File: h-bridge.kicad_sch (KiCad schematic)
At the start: 20 parts, among them J4 Conn_02x06_Counter_Clockwise, M3 DC, Q10 Q_NMOS, Q7 Q_NMOS, Q8 Q_NMOS, Q9 Q_NMOS, U11 DRV8701

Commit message: schem: add ordering info to BOM
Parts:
- C38, C39, C41: Basic (none) -> Y; JLCPCB Part # (none) -> C52923; Manufacturer (none) -> Samsung Electro-Mechanics; Manufacturer Part Number (none) -> CL05A105KA5NQNC
- C40: Basic (none) -> Y; JLCPCB Part # (none) -> C307331; Manufacturer (none) -> Samsung Electro-Mechanics; Manufacturer Part Number (none) -> CL05B104KB54PNC
- J4, M3: now left out of the parts list
- Q10, Q7, Q8, Q9: Basic (none) -> X; JLCPCB Part # (none) -> C111309; Manufacturer (none) -> Vishay Intertech; Manufacturer Part Number (none) -> SIS412DN-T1-GE3
- R41, R44, R47: Basic (none) -> Y; JLCPCB Part # (none) -> C25744; Manufacturer (none) -> Uniroyal Elec; Manufacturer Part Number (none) -> 0402WGF1002TCE
- R42: Basic (none) -> Y; JLCPCB Part # (none) -> C25779; Manufacturer (none) -> Uniroyal Elec; Manufacturer Part Number (none) -> 0402WGF3302TCE
- R43: Basic (none) -> Y; JLCPCB Part # (none) -> C25764; Manufacturer (none) -> Uniroyal Elec; Manufacturer Part Number (none) -> 0402WGF2003TCE
- R45: Basic (none) -> Y; JLCPCB Part # (none) -> C36871; Manufacturer (none) -> Uniroyal Elec; Manufacturer Part Number (none) -> 0402WGF6802TCE
- R46: footprint Resistor_SMD:R_0402_1005Metric -> Resistor_SMD:R_0603_1608Metric; Basic (none) -> Y; JLCPCB Part # (none) -> C23234; Manufacturer (none) -> Uniroyal Elec; Manufacturer Part Number (none) -> 0603WAF7501T5E
- R48: Basic (none) -> X; JLCPCB Part # (none) -> C5375467; Manufacturer (none) -> Milliohm; Manufacturer Part Number (none) -> HoYLR2512-3W-20mR-1%
- U11: Basic (none) -> X; JLCPCB Part # (none) -> C90964; Manufacturer (none) -> Texas Instruments; Manufacturer Part Number (none) -> DRV8701ERGER

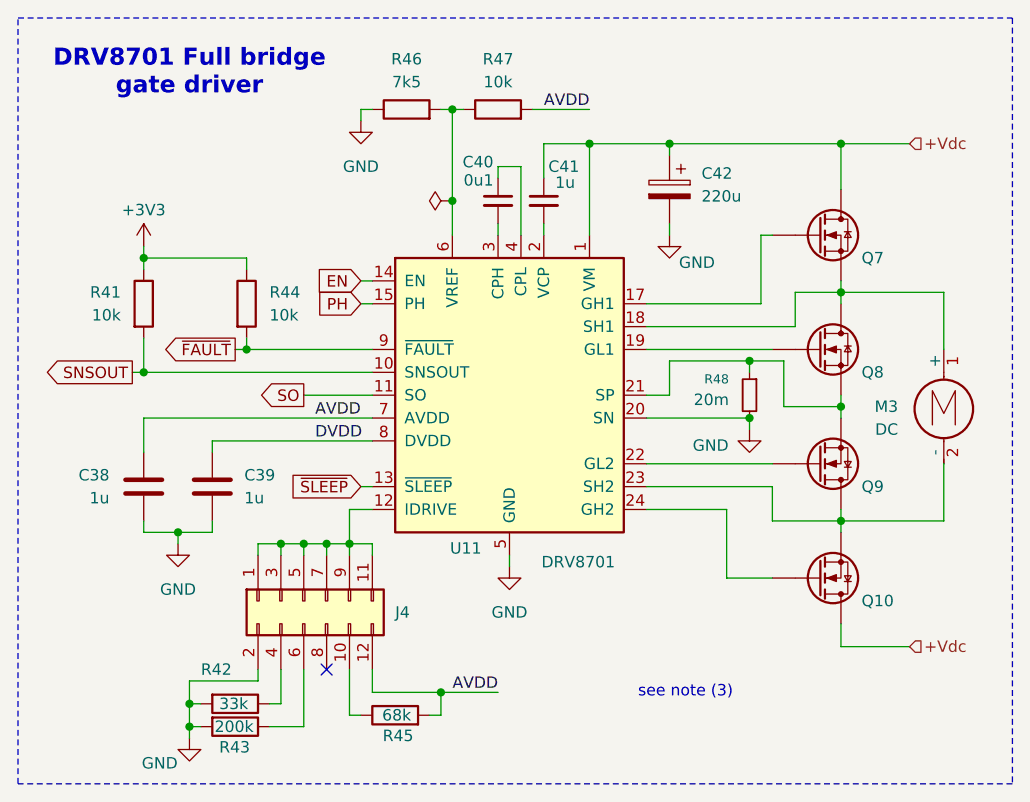
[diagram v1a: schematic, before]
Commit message: schem: renumber
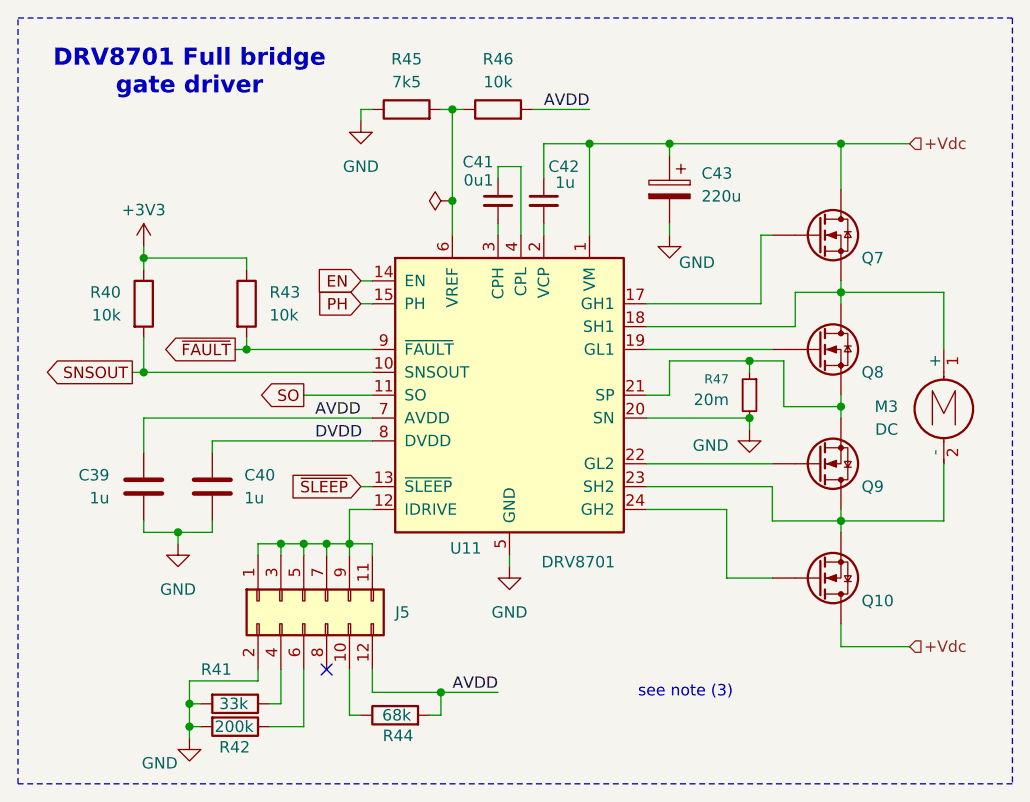
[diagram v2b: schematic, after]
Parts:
- renumbered C38 to C39, C39 to C40, C40 to C41, C41 to C42, C42 to C43, J4 to J5, R41 to R40, R42 to R41, R43 to R42, R44 to R43, R45 to R44, R46 to R45, R47 to R46, R48 to R47
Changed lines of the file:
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@@
 		(dnp no)
 		(fields_autoplaced yes)
-		(property "Reference" "#PWR082"
+		(property "Reference" "#PWR085"
 			(at 130.81 62.23 0)
 			(effects
@@
 			(project ""
 				(path "/a1dc4c9e-7b20-4b66-a693-9133bc644c6b/234f18ec-899d-4a38-bb51-5ceaab0ae171"
-					(reference "#PWR082")
+					(reference "#PWR085")
 					(unit 1)
 				)
@@
 		(on_board yes)
 		(dnp no)
-		(property "Reference" "R47"
+		(property "Reference" "R46"
 			(at 146.05 49.022 90)
 			(effects
@@
 			(project ""
 				(path "/a1dc4c9e-7b20-4b66-a693-9133bc644c6b/234f18ec-899d-4a38-bb51-5ceaab0ae171"
-					(reference "R47")
+					(reference "R46")
 					(unit 1)
 				)
@@
 		(on_board yes)
 		(dnp no)
-		(property "Reference" "C38"
+		(property "Reference" "C39"
 			(at 102.87 95.2499 0)
 			(effects
@@
 			(project ""
 				(path "/a1dc4c9e-7b20-4b66-a693-9133bc644c6b/234f18ec-899d-4a38-bb51-5ceaab0ae171"
-					(reference "C38")
+					(reference "C39")
 					(unit 1)
 				)
@@
 		(on_board yes)
 		(dnp no)
-		(property "Reference" "R43"
+		(property "Reference" "R42"
 			(at 115.062 125.476 90)
 			(effects
@@
 			(project "motor-power-poc"
 				(path "/a1dc4c9e-7b20-4b66-a693-9133bc644c6b/234f18ec-899d-4a38-bb51-5ceaab0ae171"
-					(reference "R43")
+					(reference "R42")
 					(unit 1)
 				)
@@
 		(on_board yes)
 		(dnp no)
-		(property "Reference" "C39"
+		(property "Reference" "C40"
 			(at 117.856 95.25 0)
 			(effects
@@
 			(project "motor-power-poc"
 				(path "/a1dc4c9e-7b20-4b66-a693-9133bc644c6b/234f18ec-899d-4a38-bb51-5ceaab0ae171"
-					(reference "C39")
+					(reference "C40")
 					(unit 1)
 				)
@@
 		(on_board yes)
 		(dnp no)
-		(property "Reference" "C41"
+		(property "Reference" "C42"
 			(at 151.638 60.96 0)
 			(effects
@@
 			(project "motor-power-poc"
 				(path "/a1dc4c9e-7b20-4b66-a693-9133bc644c6b/234f18ec-899d-4a38-bb51-5ceaab0ae171"
-					(reference "C41")
+					(reference "C42")
 					(unit 1)
 				)
@@
 		(on_board yes)
 		(dnp no)
-		(property "Reference" "R46"
+		(property "Reference" "R45"
 			(at 135.89 49.022 90)
 			(effects
@@
 			(project "motor-power-poc"
 				(path "/a1dc4c9e-7b20-4b66-a693-9133bc644c6b/234f18ec-899d-4a38-bb51-5ceaab0ae171"
-					(reference "R46")
+					(reference "R45")
 					(unit 1)
 				)
@@
 		(on_board yes)
 		(dnp no)
-		(property "Reference" "C42"
+		(property "Reference" "C43"
 			(at 168.656 61.722 0)
 			(effects
@@
 			(project "motor-power-poc"
 				(path "/a1dc4c9e-7b20-4b66-a693-9133bc644c6b/234f18ec-899d-4a38-bb51-5ceaab0ae171"
-					(reference "C42")
+					(reference "C43")
 					(unit 1)
 				)
@@
 		(dnp no)
 		(fields_autoplaced yes)
-		(property "Reference" "#PWR080"
+		(property "Reference" "#PWR083"
 			(at 110.49 109.22 0)
 			(effects
@@
 			(project "motor-power-poc"
 				(path "/a1dc4c9e-7b20-4b66-a693-9133bc644c6b/234f18ec-899d-4a38-bb51-5ceaab0ae171"
-					(reference "#PWR080")
+					(reference "#PWR083")
 					(unit 1)
 				)
@@
 		(on_board yes)
 		(dnp no)
-		(property "Reference" "R48"
+		(property "Reference" "R47"
 			(at 171.704 84.582 0)
 			(effects
@@
 			(project ""
 				(path "/a1dc4c9e-7b20-4b66-a693-9133bc644c6b/234f18ec-899d-4a38-bb51-5ceaab0ae171"
-					(reference "R48")
+					(reference "R47")
 					(unit 1)
 				)
@@
 		(on_board yes)
 		(dnp no)
-		(property "Reference" "R45"
+		(property "Reference" "R44"
 			(at 136.652 124.206 90)
 			(effects
@@
 			(project "motor-power-poc"
 				(path "/a1dc4c9e-7b20-4b66-a693-9133bc644c6b/234f18ec-899d-4a38-bb51-5ceaab0ae171"
-					(reference "R45")
+					(reference "R44")
 					(unit 1)
 				)
@@
 		(dnp no)
 		(fields_autoplaced yes)
-		(property "Reference" "J4"
+		(property "Reference" "J5"
 			(at 134.62 110.4899 90)
 			(effects
@@
 			(project ""
 				(path "/a1dc4c9e-7b20-4b66-a693-9133bc644c6b/234f18ec-899d-4a38-bb51-5ceaab0ae171"
-					(reference "J4")
+					(reference "J5")
 					(unit 1)
 				)
@@
 		(on_board yes)
 		(dnp no)
-		(property "Reference" "#PWR081"
+		(property "Reference" "#PWR084"
 			(at 111.76 130.81 0)
 			(effects
@@
 			(project "motor-power-poc"
 				(path "/a1dc4c9e-7b20-4b66-a693-9133bc644c6b/234f18ec-899d-4a38-bb51-5ceaab0ae171"
-					(reference "#PWR081")
+					(reference "#PWR084")
 					(unit 1)
 				)
@@
 		(on_board yes)
 		(dnp no)
-		(property "Reference" "R42"
+		(property "Reference" "R41"
 			(at 113.03 116.84 90)
 			(effects
@@
 			(project ""
 				(path "/a1dc4c9e-7b20-4b66-a693-9133bc644c6b/234f18ec-899d-4a38-bb51-5ceaab0ae171"
-					(reference "R42")
+					(reference "R41")
 					(unit 1)
 				)
@@
 		(dnp no)
 		(fields_autoplaced yes)
-		(property "Reference" "R44"
+		(property "Reference" "R43"
 			(at 120.65 74.9299 0)
 			(effects
@@
 			(project ""
 				(path "/a1dc4c9e-7b20-4b66-a693-9133bc644c6b/234f18ec-899d-4a38-bb51-5ceaab0ae171"
-					(reference "R44")
+					(reference "R43")
 					(unit 1)
 				)
@@
 		(on_board yes)
 		(dnp no)
-		(property "Reference" "C40"
+		(property "Reference" "C41"
 			(at 145.542 60.452 0)
 			(effects
@@
 			(project ""
 				(path "/a1dc4c9e-7b20-4b66-a693-9133bc644c6b/234f18ec-899d-4a38-bb51-5ceaab0ae171"
-					(reference "C40")
+					(reference "C41")
 					(unit 1)
 				)
@@
 		(on_board yes)
 		(dnp no)
-		(property "Reference" "#PWR085"
+		(property "Reference" "#PWR088"
 			(at 173.99 96.52 0)
 			(effects
@@
 			(project ""
 				(path "/a1dc4c9e-7b20-4b66-a693-9133bc644c6b/234f18ec-899d-4a38-bb51-5ceaab0ae171"
-					(reference "#PWR085")
+					(reference "#PWR088")
 					(unit 1)
 				)
@@
 		(on_board yes)
 		(dnp no)
-		(property "Reference" "#PWR084"
+		(property "Reference" "#PWR087"
 			(at 165.1 74.93 0)
 			(effects
@@
 			(project ""
 				(path "/a1dc4c9e-7b20-4b66-a693-9133bc644c6b/234f18ec-899d-4a38-bb51-5ceaab0ae171"
-					(reference "#PWR084")
+					(reference "#PWR087")
 					(unit 1)
 				)
@@
 		(on_board yes)
 		(dnp no)
-		(property "Reference" "R41"
+		(property "Reference" "R40"
 			(at 104.14 74.9299 0)
 			(effects
@@
 			(project ""
 				(path "/a1dc4c9e-7b20-4b66-a693-9133bc644c6b/234f18ec-899d-4a38-bb51-5ceaab0ae171"
-					(reference "R41")
+					(reference "R40")
 					(unit 1)
 				)
@@
 		(dnp no)
 		(fields_autoplaced yes)
-		(property "Reference" "#PWR083"
+		(property "Reference" "#PWR086"
 			(at 147.32 111.76 0)
 			(effects
@@
 			(project ""
 				(path "/a1dc4c9e-7b20-4b66-a693-9133bc644c6b/234f18ec-899d-4a38-bb51-5ceaab0ae171"
-					(reference "#PWR083")
+					(reference "#PWR086")
 					(unit 1)
 				)
@@
 		(dnp no)
 		(fields_autoplaced yes)
-		(property "Reference" "#FLG04"
+		(property "Reference" "#FLG010"
 			(at 139.065 64.77 0)
 			(effects
@@
 			(project "motor-power-poc"
 				(path "/a1dc4c9e-7b20-4b66-a693-9133bc644c6b/234f18ec-899d-4a38-bb51-5ceaab0ae171"
-					(reference "#FLG04")
+					(reference "#FLG010")
 					(unit 1)
 				)
@@
 		(on_board yes)
 		(dnp no)
-		(property "Reference" "#PWR079"
+		(property "Reference" "#PWR082"
 			(at 106.68 73.66 0)
 			(effects
@@
 			(project "motor-power-poc"
 				(path "/a1dc4c9e-7b20-4b66-a693-9133bc644c6b/234f18ec-899d-4a38-bb51-5ceaab0ae171"
-					(reference "#PWR079")
-					(unit 1)
-				)
+					(reference "#PWR082")
+					(unit 1)
+				)

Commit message: schem: update MOSFETs symbol
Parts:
- Q10, Q7, Q8, Q9: symbol Device:Q_NMOS -> Transistor_FET:SiS415DNT
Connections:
- net +Vdc: now also Q10.1 (S), Q10.2 (S), Q10.3 (S), Q7.1 (S), Q7.2 (S), Q7.3 (S); no longer Q10.D, Q7.D
- net at M3.1 (+), U11.18 (SH1): now also Q7.5 (D), Q8.1 (S), Q8.2 (S), Q8.3 (S); no longer Q7.S, Q8.D
- net at M3.2 (-), U11.23 (SH2): now also Q10.5 (D), Q9.1 (S), Q9.2 (S), Q9.3 (S); no longer Q10.S, Q9.D
- net at U11.17 (GH1): now also Q7.4 (G); no longer Q7.G
- net at R47.1, U11.21 (SP): now also Q8.5 (D), Q9.5 (D); no longer Q8.S, Q9.S
- net at U11.22 (GL2): now also Q9.4 (G); no longer Q9.G
- net at U11.24 (GH2): now also Q10.4 (G); no longer Q10.G
- net at U11.19 (GL1): now also Q8.4 (G); no longer Q8.G
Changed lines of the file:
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@@
 	)
 	(symbol
-		(lib_id "Device:Q_NMOS")
+		(lib_id "Transistor_FET:SiS415DNT")
 		(at 181.61 68.58 0)
+		(mirror x)
 		(unit 1)
 		(exclude_from_sim no)
@@
 		(dnp no)
 		(property "Reference" "Q7"
-			(at 186.436 71.12 0)
+			(at 186.436 66.04 0)
 			(effects
 				(font
@@
 		)
 		(property "Footprint" "Package_SO:Vishay_PowerPAK_1212-8_Single"
-			(at 186.69 66.04 0)
+			(at 186.69 71.12 0)
 			(effects
 				(font
@@
 			)
 		)
-		(pin "S"
-		)
-		(pin "G"
-		)
-		(pin "D"
+		(pin "3"
+		)
+		(pin "2"
+		)
+		(pin "1"
+		)
+		(pin "4"
+		)
+		(pin "5"
 		)
 		(instances
@@
 	)
 	(symbol
-		(lib_id "Device:Q_NMOS")
+		(lib_id "Transistor_FET:SiS415DNT")
 		(at 181.61 93.98 0)
-		(mirror x)
 		(unit 1)
 		(exclude_from_sim no)
@@
 		(dnp no)
 		(property "Reference" "Q9"
-			(at 186.436 96.5202 0)
+			(at 186.436 91.4398 0)
 			(effects
 				(font
@@
 		)
 		(property "Footprint" "Package_SO:Vishay_PowerPAK_1212-8_Single"
-			(at 186.69 96.52 0)
+			(at 186.69 91.44 0)
 			(effects
 				(font
@@
 			)
 		)
-		(pin "S"
-		)
-		(pin "G"
-		)
-		(pin "D"
+		(pin "4"
+		)
+		(pin "3"
+		)
+		(pin "2"
+		)
+		(pin "5"
+		)
+		(pin "1"
 		)
 		(instances
@@
 	)
 	(symbol
-		(lib_id "Device:Q_NMOS")
+		(lib_id "Transistor_FET:SiS415DNT")
 		(at 181.61 106.68 0)
-		(mirror x)
 		(unit 1)
 		(exclude_from_sim no)
@@
 		(dnp no)
 		(property "Reference" "Q10"
-			(at 186.436 109.2202 0)
+			(at 186.436 104.1398 0)
 			(effects
 				(font
@@
 		)
 		(property "Footprint" "Package_SO:Vishay_PowerPAK_1212-8_Single"
-			(at 186.69 109.22 0)
+			(at 186.69 104.14 0)
 			(effects
 				(font
@@
 			)
 		)
-		(pin "S"
-		)
-		(pin "G"
-		)
-		(pin "D"
+		(pin "4"
+		)
+		(pin "3"
+		)
+		(pin "5"
+		)
+		(pin "1"
+		)
+		(pin "2"
 		)
 		(instances
@@
 	)
 	(symbol
-		(lib_id "Device:Q_NMOS")
+		(lib_id "Transistor_FET:SiS415DNT")
 		(at 181.61 81.28 0)
+		(mirror x)
 		(unit 1)
 		(exclude_from_sim no)
@@
 		(dnp no)
 		(property "Reference" "Q8"
-			(at 186.436 83.82 0)
+			(at 186.436 78.74 0)
 			(effects
 				(font
@@
 		)
 		(property "Footprint" "Package_SO:Vishay_PowerPAK_1212-8_Single"
-			(at 186.69 78.74 0)
+			(at 186.69 83.82 0)
 			(effects
 				(font
@@
 			)
 		)
-		(pin "S"
-		)
-		(pin "G"
-		)
-		(pin "D"
-		)
-		(instances
+		(pin "4"
+		)
+		(pin "5"
+		)
+		(pin "1"
+		)
+		(pin "2"
+		)
+		(pin "3"
+		)
+		(instances

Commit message: schem: fix DRV8701 gnd pad pin number
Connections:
- net GND: now also U11.25 (GND); no longer U11.26 (GND)
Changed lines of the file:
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@@
 		(pin "15"
 		)
-		(pin "26"
+		(pin "25"
 		)
 		(pin "7"

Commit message: schem: update MOSFETs footprints to correct N-channel
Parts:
- Q10, Q7, Q8, Q9: symbol Transistor_FET:SiS415DNT -> Transistor_FET:SiS454DN
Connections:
- net +Vdc: now also Q10.5 (D), Q7.5 (D); no longer Q10.1 (S), Q10.2 (S), Q10.3 (S), Q7.1 (S), Q7.2 (S), Q7.3 (S)
- net at Q8.1 (S), Q8.2 (S), Q8.3 (S): now also Q9.1 (S), Q9.2 (S), Q9.3 (S), R47.1, U11.21 (SP); no longer M3.1 (+), Q7.5 (D), U11.18 (SH1)
- new net: M3.1 (+), Q7.1 (S), Q7.2 (S), Q7.3 (S), Q8.5 (D), U11.18 (SH1)
- new net: M3.2 (-), Q10.1 (S), Q10.2 (S), Q10.3 (S), Q9.5 (D), U11.23 (SH2)
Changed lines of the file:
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@@
 	)
 	(symbol
-		(lib_id "Transistor_FET:SiS415DNT")
+		(lib_id "Transistor_FET:SiS454DN")
 		(at 181.61 68.58 0)
-		(mirror x)
 		(unit 1)
 		(exclude_from_sim no)
@@
 		(dnp no)
 		(property "Reference" "Q7"
-			(at 186.436 66.04 0)
+			(at 186.436 71.12 0)
 			(effects
 				(font
@@
 		)
 		(property "Footprint" "Package_SO:Vishay_PowerPAK_1212-8_Single"
-			(at 186.69 71.12 0)
+			(at 186.69 66.04 0)
 			(effects
 				(font
@@
 	)
 	(symbol
-		(lib_id "Transistor_FET:SiS415DNT")
+		(lib_id "Transistor_FET:SiS454DN")
 		(at 181.61 93.98 0)
+		(mirror x)
 		(unit 1)
 		(exclude_from_sim no)
@@
 		(dnp no)
 		(property "Reference" "Q9"
-			(at 186.436 91.4398 0)
+			(at 186.436 96.5202 0)
 			(effects
 				(font
@@
 		)
 		(property "Footprint" "Package_SO:Vishay_PowerPAK_1212-8_Single"
-			(at 186.69 91.44 0)
+			(at 186.69 96.52 0)
 			(effects
 				(font
@@
 	)
 	(symbol
-		(lib_id "Transistor_FET:SiS415DNT")
+		(lib_id "Transistor_FET:SiS454DN")
 		(at 181.61 106.68 0)
+		(mirror x)
 		(unit 1)
 		(exclude_from_sim no)
@@
 		(dnp no)
 		(property "Reference" "Q10"
-			(at 186.436 104.1398 0)
+			(at 186.436 109.2202 0)
 			(effects
 				(font
@@
 		)
 		(property "Footprint" "Package_SO:Vishay_PowerPAK_1212-8_Single"
-			(at 186.69 104.14 0)
+			(at 186.69 109.22 0)
 			(effects
 				(font
@@
 	)
 	(symbol
-		(lib_id "Transistor_FET:SiS415DNT")
+		(lib_id "Transistor_FET:SiS454DN")
 		(at 181.61 81.28 0)
-		(mirror x)
 		(unit 1)
 		(exclude_from_sim no)
@@
 		(dnp no)
 		(property "Reference" "Q8"
-			(at 186.436 78.74 0)
+			(at 186.436 83.82 0)
 			(effects
 				(font
@@
 		)
 		(property "Footprint" "Package_SO:Vishay_PowerPAK_1212-8_Single"
-			(at 186.69 83.82 0)
-			(effects
-				(font
+			(at 186.69 78.74 0)
+			(effects
+				(font
